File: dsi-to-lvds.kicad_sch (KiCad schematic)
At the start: 22 parts, among them Q8 PJE138K, U2 NTS0104_DHVQFN, U3 SN65DSI84

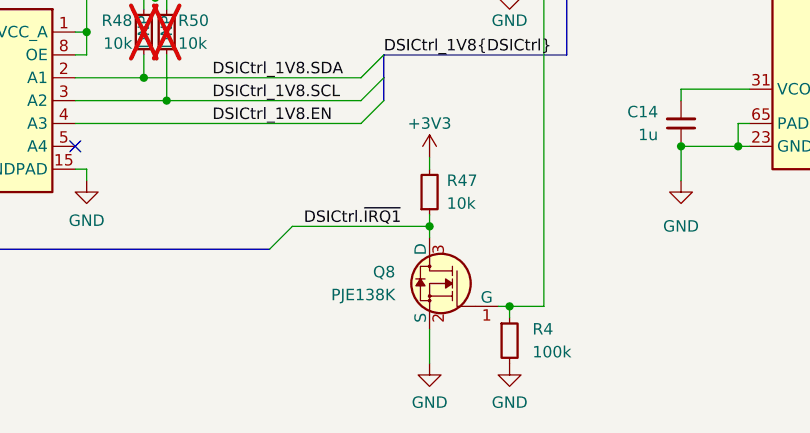
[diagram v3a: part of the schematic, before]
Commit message: [#61475] Update symbols from library & resolve ERC issues
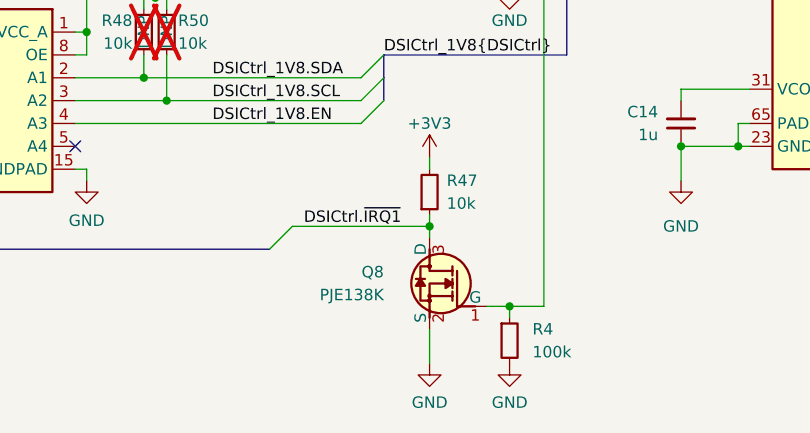
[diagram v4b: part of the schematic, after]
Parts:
- C10, C11, C12, C13, C14, C4, C5, C6, C7, C8, C9, FB1, R4, R47, R48, R50, R6, R7, R8: Public (none) -> False
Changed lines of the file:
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@@
     (stroke (width 0) (type default))
   )
-  (wire (pts (xy 165.1 153.67) (xy 166.37 153.67))
+  (wire (pts (xy 163.83 153.67) (xy 166.37 153.67))
     (stroke (width 0) (type default))
   )
@@
     (property "DNP" "DNP" (at 166.37 106.68 0)
       (effects (font (size 1.27 1.27)))
+    )
+    (property "Public" "False" (at 135.89 88.9 0)
+      (effects (font (size 1.27 1.27)) (justify left bottom) hide)
     )
     (pin "1")
@@
       (effects (font (size 1.27 1.27)) (justify left bottom) hide)
     )
+    (property "Public" "False" (at 209.55 39.37 0)
+      (effects (font (size 1.27 1.27)) (justify left bottom) hide)
+    )
     (pin "1")
     (pin "2")
@@
     )
     (property "Dielectric" "X7R" (at 198.12 39.37 0)
+      (effects (font (size 1.27 1.27)) (justify left bottom) hide)
+    )
+    (property "Public" "False" (at 200.66 39.37 0)
       (effects (font (size 1.27 1.27)) (justify left bottom) hide)
     )
@@
       (effects (font (size 1.27 1.27)) (justify left bottom) hide)
     )
+    (property "Public" "False" (at 152.4 115.57 0)
+      (effects (font (size 1.27 1.27)) (justify left bottom) hide)
+    )
     (pin "1")
     (pin "2")
@@
       (effects (font (size 1.27 1.27)) (justify left bottom) hide)
     )
+    (property "Public" "False" (at 165.1 39.37 0)
+      (effects (font (size 1.27 1.27)) (justify left bottom) hide)
+    )
     (pin "1")
     (pin "2")
@@
     )
     (property "Tolerance" "1%" (at 156.21 96.52 0)
+      (effects (font (size 1.27 1.27)) (justify left bottom) hide)
+    )
+    (property "Public" "False" (at 135.89 96.52 0)
       (effects (font (size 1.27 1.27)) (justify left bottom) hide)
     )
@@
       (effects (font (size 1.27 1.27)) (justify left bottom) hide)
     )
+    (property "Public" "False" (at 81.28 83.82 0)
+      (effects (font (size 1.27 1.27)) (justify left bottom) hide)
+    )
     (pin "1")
     (pin "2")
@@
       (effects (font (size 1.27 1.27)) (justify left bottom) hide)
     )
+    (property "Public" "False" (at 156.21 39.37 0)
+      (effects (font (size 1.27 1.27)) (justify left bottom) hide)
+    )
     (pin "1")
     (pin "2")
@@
       (effects (font (size 1.27 1.27)))
     )
+    (property "Public" "False" (at 95.25 105.41 0)
+      (effects (font (size 1.27 1.27)) (justify left bottom) hide)
+    )
     (pin "1")
     (pin "2")
@@
       (effects (font (size 1.27 1.27)) (justify left bottom) hide)
     )
+    (property "Public" "False" (at 190.5 39.37 0)
+      (effects (font (size 1.27 1.27)) (justify left bottom) hide)
+    )
     (pin "1")
     (pin "2")
@@
     )
     (property "Dielectric" "X5R" (at 170.18 39.37 0)
+      (effects (font (size 1.27 1.27)) (justify left bottom) hide)
+    )
+    (property "Public" "False" (at 172.72 39.37 0)
       (effects (font (size 1.27 1.27)) (justify left bottom) hide)
     )
@@
       (effects (font (size 1.27 1.27)) hide)
     )
+    (property "Public" "False" (at 135.89 67.31 0)
+      (effects (font (size 1.27 1.27)) (justify left bottom) hide)
+    )
     (pin "1")
     (pin "2")
@@
     )
     (property "Dielectric" "X7R" (at 215.9 39.37 0)
+      (effects (font (size 1.27 1.27)) (justify left bottom) hide)
+    )
+    (property "Public" "False" (at 218.44 39.37 0)
       (effects (font (size 1.27 1.27)) (justify left bottom) hide)
     )
@@
       (effects (font (size 1.27 1.27)) (justify left bottom) hide)
     )
+    (property "Public" "False" (at 166.37 132.08 0)
+      (effects (font (size 1.27 1.27)) (justify left bottom) hide)
+    )
     (pin "1")
     (pin "2")
@@
     )
   )
-  (symbol (lib_id "antmicroTransistorsFETsMOSFETsSingle:PJE138K") (at 165.1 153.67 0) (mirror y) (unit 1)
-    (in_bom yes) (on_board yes) (dnp no) (fields_autoplaced)
-    (property "Reference" "Q8" (at 153.67 149.86 0)
+  (symbol (lib_id "antmicroTransistorsFETsMOSFETsSingle:PJE138K") (at 163.83 153.67 0) (mirror y) (unit 1)
+    (in_bom yes) (on_board yes) (dnp no) (fields_autoplaced)
+    (property "Reference" "Q8" (at 152.4 149.86 0)
       (effects (font (size 1.27 1.27) (thickness 0.15)) (justify left))
     )
-    (property "Value" "PJE138K" (at 153.67 152.4 0)
+    (property "Value" "PJE138K" (at 152.4 152.4 0)
       (effects (font (size 1.27 1.27) (thickness 0.15)) (justify left))
     )
-    (property "Footprint" "antmicro-footprints:SOT-523" (at 142.24 165.1 0)
-      (effects (font (size 1.27 1.27) (thickness 0.15)) (justify left bottom) hide)
-    )
-    (property "Datasheet" "https://www.mouser.com/datasheet/2/1057/PJE138K-1876698.pdf" (at 142.24 167.64 0)
-      (effects (font (size 1.27 1.27) (thickness 0.15)) (justify left bottom) hide)
-    )
-    (property "MPN" "PJE138K_R1_00001" (at 142.24 170.18 0)
-      (effects (font (size 1.27 1.27) (thickness 0.15)) (justify left bottom) hide)
-    )
-    (property "Manufacturer" "PANJIT" (at 142.24 172.72 0)
-      (effects (font (size 1.27 1.27) (thickness 0.15)) (justify left bottom) hide)
-    )
-    (property "Author" "Antmicro" (at 142.24 175.26 0)
-      (effects (font (size 1.27 1.27) (thickness 0.15)) (justify left bottom) hide)
-    )
-    (property "License" "Apache-2.0" (at 142.24 177.8 0)
+    (property "Footprint" "antmicro-footprints:SOT-523" (at 140.97 165.1 0)
+      (effects (font (size 1.27 1.27) (thickness 0.15)) (justify left bottom) hide)
+    )
+    (property "Datasheet" "https://www.mouser.com/datasheet/2/1057/PJE138K-1876698.pdf" (at 140.97 167.64 0)
+      (effects (font (size 1.27 1.27) (thickness 0.15)) (justify left bottom) hide)
+    )
+    (property "MPN" "PJE138K_R1_00001" (at 140.97 170.18 0)
+      (effects (font (size 1.27 1.27) (thickness 0.15)) (justify left bottom) hide)
+    )
+    (property "Manufacturer" "PANJIT" (at 140.97 172.72 0)
+      (effects (font (size 1.27 1.27) (thickness 0.15)) (justify left bottom) hide)
+    )
+    (property "Author" "Antmicro" (at 140.97 175.26 0)
+      (effects (font (size 1.27 1.27) (thickness 0.15)) (justify left bottom) hide)
+    )
+    (property "License" "Apache-2.0" (at 140.97 177.8 0)
       (effects (font (size 1.27 1.27) (thickness 0.15)) (justify left bottom) hide)
     )
@@
       (effects (font (size 1.27 1.27)) (justify left bottom) hide)
     )
+    (property "Public" "False" (at 69.85 83.82 0)
+      (effects (font (size 1.27 1.27)) (justify left bottom) hide)
+    )
     (pin "1")
     (pin "2")
@@
     )
     (property "Dielectric" "X5R" (at 179.07 39.37 0)
+      (effects (font (size 1.27 1.27)) (justify left bottom) hide)
+    )
+    (property "Public" "False" (at 181.61 39.37 0)
       (effects (font (size 1.27 1.27)) (justify left bottom) hide)
     )
@@
       (effects (font (size 1.27 1.27)))
     )
+    (property "Public" "False" (at 158.75 105.41 0)
+      (effects (font (size 1.27 1.27)) (justify left bottom) hide)
+    )
     (pin "1")
     (pin "2")
@@
       (effects (font (size 1.27 1.27)) (justify left bottom) hide)
     )
+    (property "Public" "False" (at 187.96 123.19 0)
+      (effects (font (size 1.27 1.27)) (justify left bottom) hide)
+    )
     (pin "1")
     (pin "2")
@@
       (effects (font (size 1.27 1.27)) (justify left bottom) hide)
     )
+    (property "Public" "False" (at 196.85 175.26 0)
+      (effects (font (size 1.27 1.27)) (justify left bottom) hide)
+    )
